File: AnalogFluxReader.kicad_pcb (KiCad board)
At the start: 2 copper layers, 56 parts, among them J1 Conn_02x10_Odd_Even, J2 Conn_02x10_Odd_Even, J3 , J4 FLOPPY+, J5 FLOPPY-GND, J6 FLOPPY-, U1 AD9235BR, U2 74AC163, U3 AD8138, U4 74HC14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

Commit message: Layout done. Some fixes to schematic.
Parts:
- added C19: 100n, Capacitor_SMD:C_0805_2012Metric_Pad1.15x1.40mm_HandSolder, B.Cu at (128.3, 95.5)
- added C20: 100n, Capacitor_SMD:C_0805_2012Metric_Pad1.15x1.40mm_HandSolder, B.Cu at (128.4, 93.2)
- added C21: 100n, Capacitor_SMD:C_0805_2012Metric_Pad1.15x1.40mm_HandSolder, B.Cu at (125.8, 79.9)
- added C22: 100n, Capacitor_SMD:C_0805_2012Metric_Pad1.15x1.40mm_HandSolder, B.Cu at (102.4, 79.7)
- added REF**: MountingHole_3.2mm_M3, MountingHole:MountingHole_3.2mm_M3, F.Cu at (99.1, 109.2)
- added REF**: MountingHole_3.2mm_M3, MountingHole:MountingHole_3.2mm_M3, F.Cu at (99.1, 44.5)
- added REF**: MountingHole_3.2mm_M3, MountingHole:MountingHole_3.2mm_M3, F.Cu at (132.1, 44.5)
- added REF**: MountingHole_3.2mm_M3, MountingHole:MountingHole_3.2mm_M3, F.Cu at (139.7, 95.2)
- C13, C14, C15, C17, C18, C4, C5, C7, C8, R1, R2, R4: moved to B.Cu
- J3: value (none) -> Conn_02x05_Top_Bottom
- moved C6 71.3 mm to (95.6, 65.9), turned to 270 degrees
- moved R3 69.4 mm to (108.5, 64.9)
- moved U5 68.9 mm to (102.5, 79.6), turned to 90 degrees
- moved R21 66.9 mm to (96.8, 60.4), turned to 270 degrees
- moved C5 66.5 mm to (110.9, 54.3), turned to 270 degrees
- moved R17 66.2 mm to (108.5, 71.6)
- moved R16 62.3 mm to (108.5, 67.1)
- moved R2 62.2 mm to (105.1, 93.4)
- moved C17 59.4 mm to (119.9, 54.4), turned to 270 degrees
- moved C7 58.9 mm to (114.3, 79.6)
- moved R22 57.8 mm to (122.7, 61.4)
- moved R14 56.8 mm to (108.5, 69.3)
- moved J5 56.3 mm to (127.0, 110.5)
- moved J6 56.0 mm to (133.3, 110.5)
- moved U6 55.9 mm to (102.8, 98.0)
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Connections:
- J1 pad 1: /SECTOR -> /INDEX
- J1 pad 10: +3V3 -> Net-(J1-Pad10)
- J1 pad 11: GND -> Net-(J1-Pad11)
- J1 pad 12: /IFCLK -> Net-(J1-Pad12)
- J1 pad 13: /SCL -> /RESET
- J1 pad 14: /SDA -> Net-(J1-Pad14)
- J1 pad 15: /PB0 -> Net-(J1-Pad15)
- J1 pad 16: /PB1 -> Net-(J1-Pad16)
- J1 pad 17: /PB2 -> /PB7
- J1 pad 18: /PB3 -> /PB6
- J1 pad 19: GND -> /PB5
- J1 pad 2: Net-(J1-Pad2) -> /PD1
- J1 pad 20: +3V3 -> /PB4
- J1 pad 3: Net-(J1-Pad3) -> /PD2
- J1 pad 4: GND -> /PD3
- J1 pad 5: /CLK -> /PD0
- J1 pad 6: GND -> Net-(J1-Pad6)
- J1 pad 7: GND -> Net-(J1-Pad7)
- J2 pad 1: /INDEX -> /SECTOR
- J2 pad 10: Net-(J2-Pad10) -> +3V3
- J2 pad 11: Net-(J2-Pad11) -> GND
- J2 pad 12: Net-(J2-Pad12) -> /IFCLK
- J2 pad 13: /RESET -> /SCL
- J2 pad 14: Net-(J2-Pad14) -> /SDA
- J2 pad 15: Net-(J2-Pad15) -> /PB0
- J2 pad 16: Net-(J2-Pad16) -> /PB1
- J2 pad 17: /PB7 -> /PB2
- J2 pad 18: /PB6 -> /PB3
- J2 pad 19: /PB5 -> GND
- J2 pad 2: /PD1 -> Net-(J2-Pad2)
- J2 pad 20: /PB4 -> +3V3
- J2 pad 3: /PD2 -> Net-(J2-Pad3)
- J2 pad 4: /PD3 -> GND
- J2 pad 5: /PD0 -> /CLK
- J2 pad 6: Net-(J2-Pad6) -> GND
- J2 pad 7: Net-(J2-Pad7) -> GND
- R1 pad 2: Net-(J3-Pad8) -> Net-(J3-Pad9)
- R19 pad 1: Net-(J2-Pad11) -> Net-(J1-Pad11)
- R2 pad 2: Net-(J3-Pad6) -> Net-(J3-Pad8)
- R20 pad 1: Net-(J2-Pad8) -> Net-(J1-Pad8)
- R21 pad 1: Net-(J1-Pad8) -> Net-(J2-Pad8)
- R4 pad 2: Net-(J3-Pad2) -> Net-(J3-Pad6)
- U4 pad 1: Net-(J3-Pad2) -> Net-(J3-Pad6)
- U4 pad 10: (no net) -> Net-(U4-Pad10)
- U4 pad 11: (no net) -> GND
- U4 pad 12: (no net) -> Net-(U4-Pad12)
- U4 pad 13: (no net) -> GND
- U4 pad 3: (no net) -> Net-(J3-Pad8)
- U4 pad 4: (no net) -> /SECTOR
- U4 pad 5: Net-(J3-Pad6) -> Net-(J3-Pad9)
- U4 pad 6: /SECTOR -> /INDEX
- U4 pad 8: /INDEX -> Net-(U4-Pad8)
- U4 pad 9: Net-(J3-Pad8) -> GND
- U5 pad 10: Net-(J3-Pad9) -> Net-(J3-Pad4)
- U5 pad 12: (no net) -> Net-(U5-Pad12)
- U5 pad 13: (no net) -> GND
- U5 pad 4: Net-(J3-Pad3) -> Net-(J3-Pad2)
- U5 pad 6: Net-(J3-Pad5) -> Net-(J3-Pad3)
- U5 pad 8: Net-(J3-Pad7) -> Net-(J3-Pad5)
- U8 pad 3: Net-(U2-Pad11) -> Net-(U2-Pad14)
- U8 pad 4: Net-(U2-Pad12) -> Net-(U2-Pad13)
- U8 pad 5: Net-(U2-Pad13) -> Net-(U2-Pad12)
- U8 pad 6: Net-(U2-Pad14) -> Net-(U2-Pad11)
- U9 pad 21: Net-(U9-Pad21) -> GND
- U9 pad 22: Net-(U9-Pad22) -> GND
- U9 pad 23: Net-(U9-Pad23) -> GND
- U9 pad 24: Net-(U9-Pad24) -> GND
- U9 pad 25: Net-(U9-Pad25) -> GND
- U9 pad 26: Net-(U9-Pad26) -> GND
- U9 pad 27: Net-(U9-Pad27) -> GND
- U9 pad 28: Net-(U9-Pad28) -> GND
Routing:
- net GND: track 0.00 -> 324.1 mm, vias 0 -> 24
- net +3V3: track 0.00 -> 238.8 mm, vias 0 -> 14
- net GNDA: track 0.00 -> 113.4 mm, vias 0 -> 3
- net /IFCLK: track 0.00 -> 79.2 mm, vias 0 -> 4
- net /SECTOR: track 0.00 -> 53.1 mm, vias 0 -> 1
- net /INDEX: track 0.00 -> 52.8 mm, vias 0 -> 2
- net /PB0: track 0.00 -> 44.9 mm, vias 0 -> 1
- net /PB2: track 0.00 -> 42.7 mm, vias 0 -> 1
- net /PB1: track 0.00 -> 39.2 mm, vias 0 -> 1
- net /PB3: track 0.00 -> 39.1 mm, vias 0 -> 1
- net +3.3VADC: track 0.00 -> 38.3 mm, vias 0 -> 3
- net /PD1: track 0.00 -> 34.0 mm, vias 0 -> 1
- net /HEADLOAD: track 0.00 -> 33.7 mm
- net /PD3: track 0.00 -> 32.5 mm
- net /PD2: track 0.00 -> 29.8 mm, vias 0 -> 1
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- added copper zone on B.Cu, net GND
- added copper zone on F.Cu, net GND
- added copper zone on B.Cu, net GNDA
- added copper zone on F.Cu, net GNDA
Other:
- board outline added: 50.8 x 72.4 mm
- net class PWR added: clearance 0.2, trace_width 0.4, via_dia 0.8, via_drill 0.4

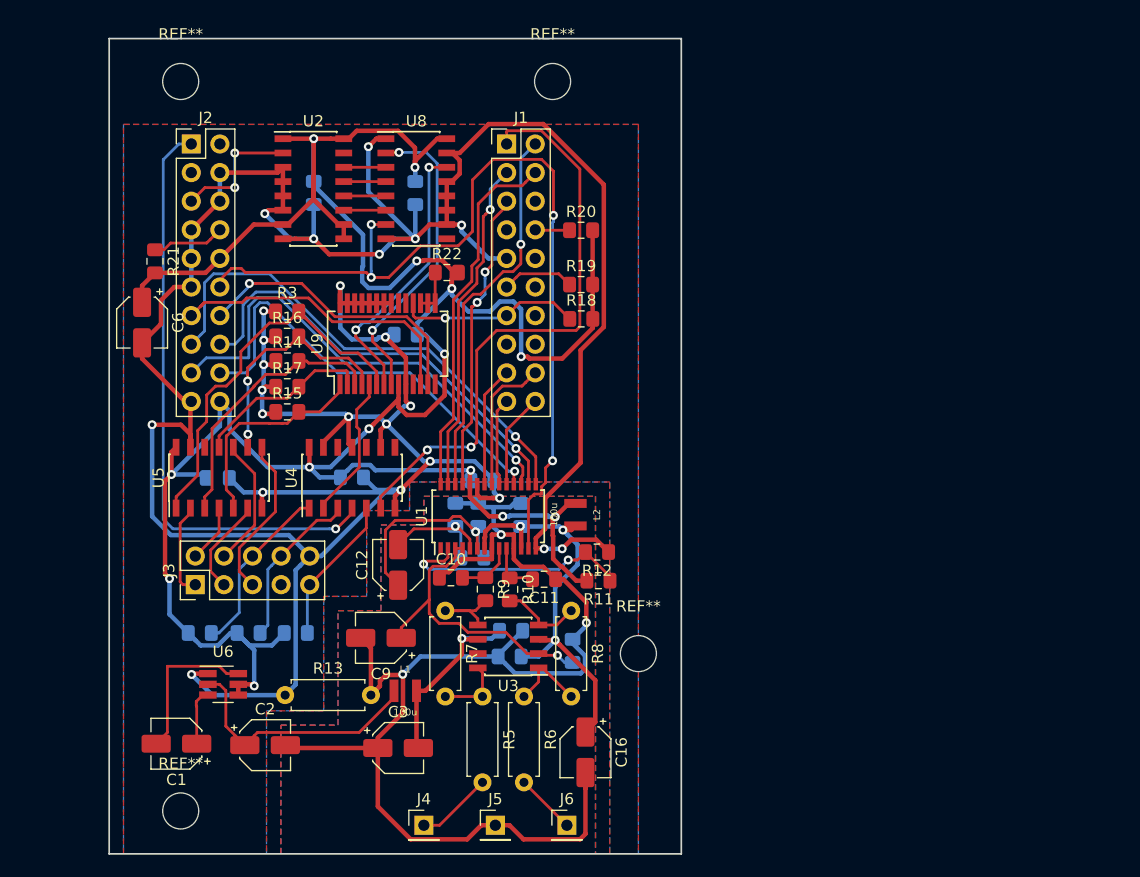
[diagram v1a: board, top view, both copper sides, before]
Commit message: Review found some issues.
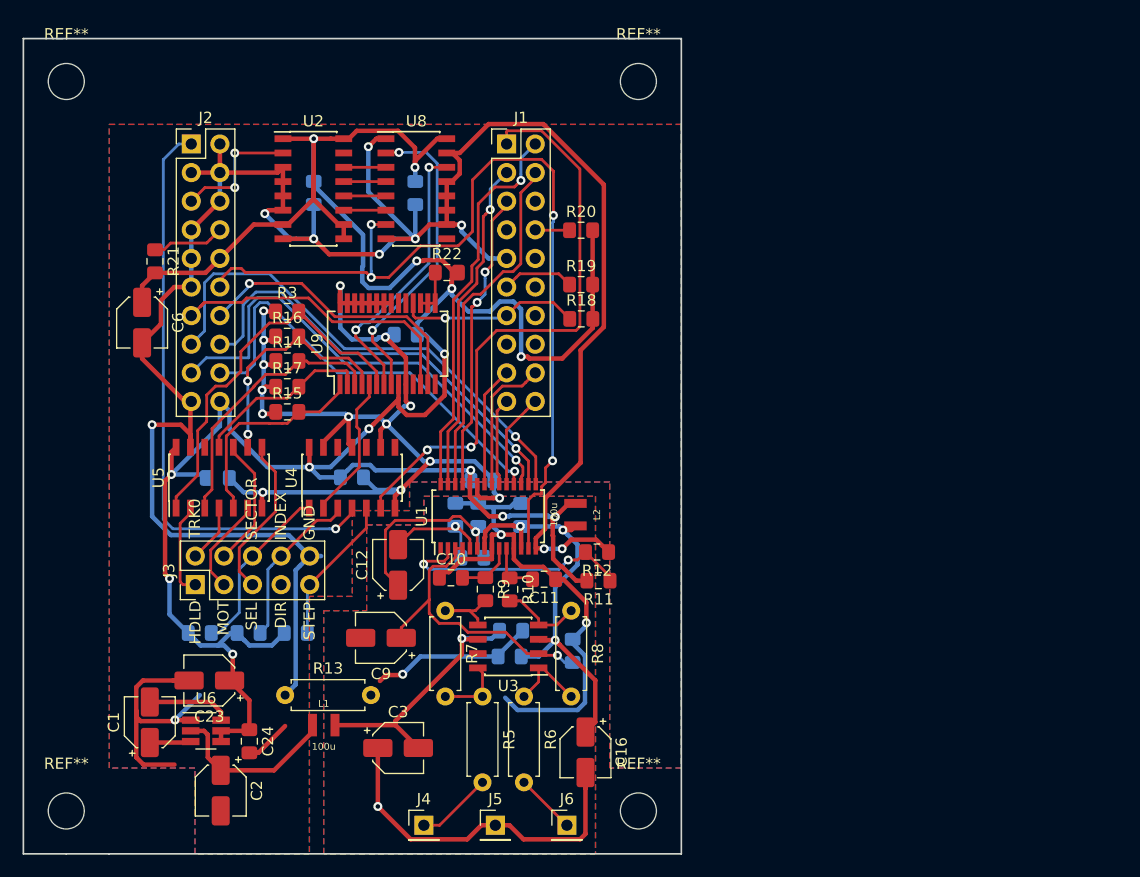
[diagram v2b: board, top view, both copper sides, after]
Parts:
- removed the REF** at (99.1, 109.2)
- removed the REF** at (99.1, 44.5)
- removed the REF** at (132.1, 44.5)
- removed the REF** at (139.7, 95.2)
- added C23: 3.3u, Capacitor_SMD:CP_Elec_4x5.4, F.Cu at (101.6, 97.6)
- added C24: 100n, Capacitor_SMD:C_0805_2012Metric_Pad1.15x1.40mm_HandSolder, F.Cu at (105.2, 103.0)
- added REF**: MountingHole_3.2mm_M3, MountingHole:MountingHole_3.2mm_M3, F.Cu at (88.9, 44.5)
- added REF**: MountingHole_3.2mm_M3, MountingHole:MountingHole_3.2mm_M3, F.Cu at (139.7, 44.5)
- added REF**: MountingHole_3.2mm_M3, MountingHole:MountingHole_3.2mm_M3, F.Cu at (139.7, 109.2)
- added REF**: MountingHole_3.2mm_M3, MountingHole:MountingHole_3.2mm_M3, F.Cu at (88.9, 109.2)
- moved L1 7.85 mm to (111.8, 101.6)
- moved C2 5.64 mm to (102.6, 107.4), turned to 270 degrees
- moved U6 4.40 mm to (101.3, 102.1)
- moved C1 3.03 mm to (96.3, 101.3), turned to 90 degrees
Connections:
- C2 pad 2: GNDA -> GND
- J1 pad 2: /PD1 -> /PD3
- J1 pad 4: /PD3 -> /PD1
- J2 pad 2: Net-(J2-Pad2) -> GND
- J2 pad 3: Net-(J2-Pad3) -> GND
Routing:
- net GNDA: track 113.4 -> 93.1 mm, vias 3 -> 4
- net GND: track 324.1 -> 338.0 mm
- net Net-(C2-Pad1): track 23.0 -> 15.5 mm
- net -3V3: track 17.0 -> 23.7 mm
- net Net-(C1-Pad2): track 13.8 -> 7.42 mm
- net +3V3: track 238.8 -> 243.7 mm
- net /PD1: track 34.0 -> 31.5 mm, vias 1 -> 0
- net /PD3: track 32.5 -> 34.7 mm, vias 0 -> 1
- net Net-(C1-Pad1): track 5.03 -> 3.66 mm
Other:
- board size 50.8 x 72.4 mm -> 58.4 x 72.4 mm
- board text added: "DIR"
- board text added: "GND"
- board text added: "HDLD"
- board text added: "INDEX"
- board text added: "MOT"
- board text added: "Mattis Lind 2021"
- board text added: "SECTOR"
- board text added: "SEL"
- board text added: "STEP"
- board text added: "TRK0"
- board text added: "https://github.com/MattisLind/AnalogFluxReader"
- board text added: "www.datormuseum.se"
